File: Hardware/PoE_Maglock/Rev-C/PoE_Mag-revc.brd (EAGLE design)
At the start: 91.8 x 45.4 mm, 82 parts, among them IC2 ATMEGA32U4-MU, J2 1X2-3.5MM, J3 1X2-3.5MM, J4 1X2-3.5MM, J5 1X2-3.5MM, J6 10103594-0001LF, Q1 35A/25V/8.5mΩ, Q3 35A/25V/8.5mΩ, Q5 35A/25V/8.5mΩ, Q6 35A/25V/8.5mΩ, SW1 SPST_TACT-KMR2, T1 DMG3415U, U2 SPX3819-3.3, U3 LMV358IDGKR, U4 W5500, U6 V_REG_317DPACK, X2 J1011FHANRUN, Y4 8MHz

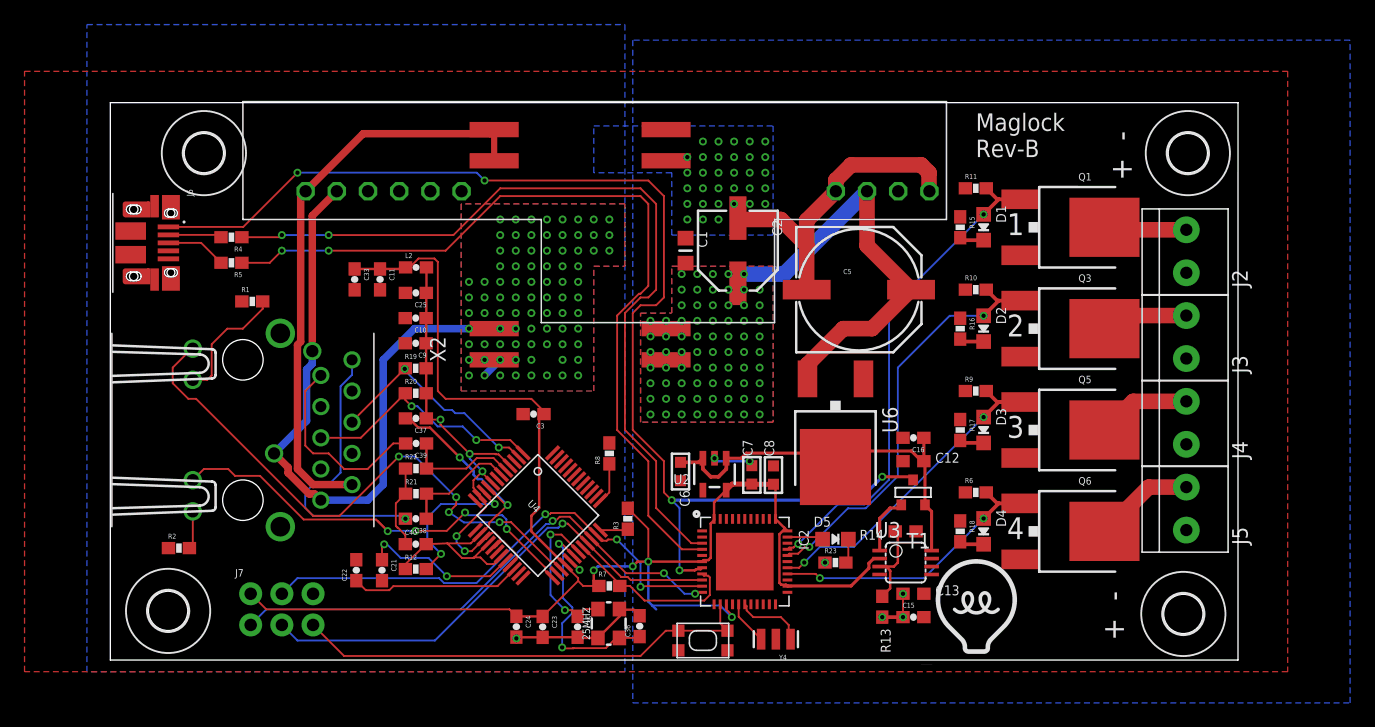
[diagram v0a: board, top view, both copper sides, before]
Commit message: almost done with maglock, adjusted PoE tDocu footprint
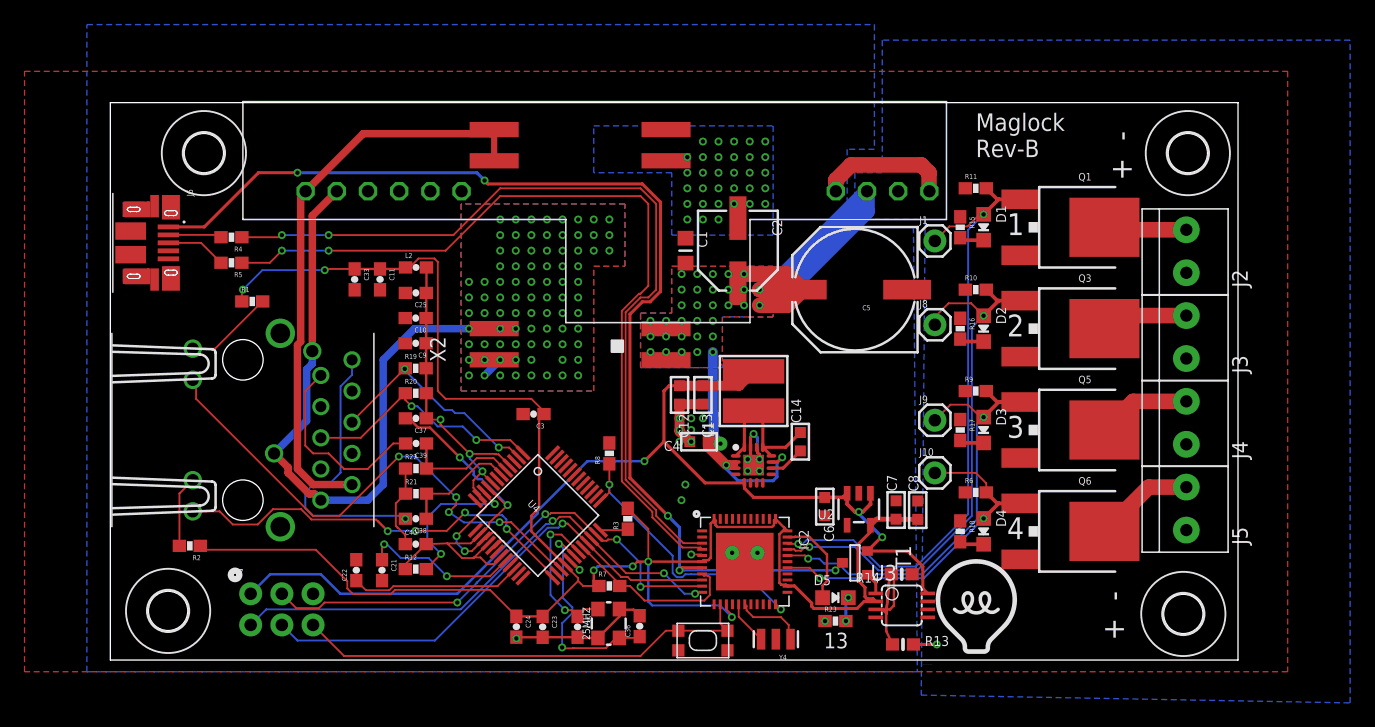
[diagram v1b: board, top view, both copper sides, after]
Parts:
- removed C15, C16: 10uF, SparkFun-Passives:0603-CAP
- removed U6: V_REG_317DPACK, SparkFun-IC-Power:V-REG_DPACK
- added C14: 22nF, microbuilder:0603-MINI
- added C4: 10µF 50V, microbuilder:0603-MINI
- added J1, J10, J8, J9: (no value), SparkFun-Connectors:1X01
- added L1: 4.7uH, microbuilder:INDUCTOR_5X5MM_TDK_VLC5045
- added U$19: BUCK_CONVERTER, Heep:QFN-16
- C12, C13: value 0.1uF -> 22uF 10V; device microbuilder:0603-NO -> microbuilder:0603-MINI
- moved C13 23.6 mm to (48.9, 21.9), turned to 270 degrees
- moved C12 19.8 mm to (47.0, 21.9), turned to 270 degrees
- moved C7 12.1 mm to (64.6, 12.5)
- moved U2 12.1 mm to (61.6, 12.6)
- moved C6 12.1 mm to (58.8, 12.8)
- moved C8 12.1 mm to (66.4, 12.5)
- moved T1 7.44 mm to (61.3, 8.26), turned to 270 degrees
- moved R23 4.76 mm to (59.7, 3.49)
- moved D5 4.76 mm to (59.7, 5.40)
- moved U3 3.51 mm to (65.1, 4.76)
- moved R14 3.51 mm to (65.1, 7.30)
- moved R13 3.51 mm to (65.2, 1.59), turned to 0 degrees
- moved R2 0.91 mm to (7.11, 9.62), turned to 180 degrees
- moved C5 0.32 mm to (61.3, 30.5), turned to 180 degrees
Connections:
- removed net 5: IC2.31
- removed net WIZ_RST_WIZ: R8.1, U4.37
- new net N$14: C14.1, U$19.P10
- new net N$15: C14.2, L1.P$1, U$19.P1, U$19.P12, U$19.P13, U$19.P16
- net +3V3: now also R1.1, R2.1; no longer J7.2
- net +5V: now also C12.1, C13.1, J7.2, L1.P$2, U$19.P5; no longer C12.2, C16.1, U6.4
- net ACTLED: now also X2.12; no longer X2.11
- net EN1: now also IC2.31, J1.1; no longer IC2.30
- net EN2: now also IC2.30, J8.1; no longer IC2.29
- net EN3: now also IC2.29, J9.1; no longer IC2.27
- net EN4: now also IC2.27, J10.1; no longer IC2.26
- net GND: now also C12.2, C4.2, U$19.P14, U$19.P15, U$19.P4, U$19.PAD; no longer C12.1, C15.2, C16.2, R1.1, R2.1, U6.1
- net LNKLED: now also X2.14; no longer X2.13
- net N$3: now also X2.13; no longer X2.14
- net N$4: now also X2.11; no longer X2.12
- net VBAT: now also C4.1, U$19.P11, U$19.P2, U$19.P3; no longer C13.1, C15.1, U6.3
- net WIZ_RST: now also R8.1, U4.37
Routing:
- net +5V: track 33.2 -> 86.4 mm, vias 0 -> 3
- net VBAT: track 38.0 -> 62.7 mm, vias 76 -> 36
- net +3V3: track 130.6 -> 155.1 mm, vias 4 -> 6
- net WIZ_RST: track 0.00 -> 23.5 mm, vias 0 -> 2
- net N$15: track 0.00 -> 12.1 mm
- net EN1: track 40.3 -> 52.3 mm
- net EN2: track 34.1 -> 44.8 mm
- net EN3: track 27.6 -> 37.9 mm
- net GND: track 75.6 -> 67.1 mm, vias 39 -> 54
- net VBUS: track 99.5 -> 91.4 mm
- net CMP: track 7.06 -> 14.2 mm
- net EN4: track 23.0 -> 28.5 mm
- net 13: track 2.93 -> 7.49 mm
- net ACTLED: track 47.0 -> 42.6 mm
- net WIZ_RST_WIZ: track 3.33 -> 0.00 mm
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
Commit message: ready for dylan review
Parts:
- added J11, J12: (no value), SparkFun-Connectors:1X04
- added J13: (no value), SparkFun-Connectors:1X04_NO_SILK
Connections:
- net +3V3: now also J12.1, J12.2, J12.3, J12.4
- net A0: now also J13.4
- net A1: now also J13.3
- net A2: now also J13.2
- net A3: now also J13.1
- net GND: now also J11.1, J11.2, J11.3, J11.4
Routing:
- net A3: track 0.00 -> 20.0 mm, vias 0 -> 1
- net +3V3: track 155.1 -> 173.0 mm
- net A2: track 0.00 -> 15.8 mm, vias 0 -> 1
- net A1: track 0.00 -> 12.4 mm, vias 0 -> 1
- net A0: track 0.00 -> 11.2 mm, vias 0 -> 1
- net GND: vias 54 -> 55
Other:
- board text added: "Maglock Rev-C"
- board text removed: "Maglock Rev-B"
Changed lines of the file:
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@@
 <setting verticaltext="up"/>
 </settings>
-<grid distance="0.15875" unitdist="mm" unit="mm" style="lines" multiple="1" display="no" altdistance="0.15875" altunitdist="mm" altunit="mm"/>
+<grid distance="0.003125" unitdist="mic" unit="mm" style="lines" multiple="1" display="no" altdistance="0.15875" altunitdist="mm" altunit="mm"/>
 <layers>
 <layer number="1" name="Top" color="4" fill="1" visible="yes" active="yes"/>
@@
 <text x="83.82" y="39.37" size="1.778" layer="21" rot="R90">+  -</text>
 <text x="71.12" y="41.275" size="1.4224" layer="21">Maglock
-Rev-B</text>
+Rev-C</text>
 <circle x="10.795" y="7.25" radius="0.25" width="0.7" layer="21"/>
 <text x="58.7375" y="1.27" size="1.27" layer="21" font="fixed" ratio="10" distance="100">13</text>
@@
 <element name="J9" library="SparkFun-Connectors" package="1X01" value="" x="67.78625" y="19.84375"/>
 <element name="J10" library="SparkFun-Connectors" package="1X01" value="" x="67.78625" y="15.5575"/>
+<element name="J11" library="SparkFun-Connectors" package="1X04" value="" x="64.77" y="16.1925" rot="R90">
+<attribute name="PROD_ID" value="CONN-09696" x="64.77" y="16.1925" size="1.778" layer="27" rot="R90" display="off"/>
+</element>
+<element name="J12" library="SparkFun-Connectors" package="1X04" value="" x="59.69" y="16.1925" rot="R90">
+<attribute name="PROD_ID" value="CONN-09696" x="59.69" y="16.1925" size="1.778" layer="27" rot="R90" display="off"/>
+</element>
+<element name="J13" library="SparkFun-Connectors" package="1X04_NO_SILK" value="" x="62.23" y="23.8125" rot="R270">
+<attribute name="PROD_ID" value="CONN-09696" x="62.23" y="23.8125" size="1.778" layer="27" rot="R270" display="off"/>
+</element>
 </elements>
 <signals>
@@
 <via x="47.14875" y="13.335" extent="1-16" drill="0.35"/>
 <via x="47.46625" y="14.605" extent="1-16" drill="0.35"/>
+<contactref element="J11" pad="4"/>
+<contactref element="J11" pad="3"/>
+<contactref element="J11" pad="2"/>
+<contactref element="J11" pad="1"/>
+<via x="56.605040625" y="11.79225625" extent="1-16" drill="0.35"/>
 </signal>
 <signal name="RD-">
@@
 <signal name="A3">
 <contactref element="IC2" pad="39"/>
+<contactref element="J13" pad="1"/>
+<via x="51.634425" y="13.98578125" extent="1-16" drill="0.35"/>
+<wire x1="51.634425" y1="13.98578125" x2="52.21554375" y2="14.5669" width="0.1524" layer="16"/>
+<wire x1="52.21554375" y1="14.5669" x2="54.7573" y2="14.5669" width="0.1524" layer="16"/>
+<wire x1="54.7573" y1="14.5669" x2="56.74471875" y2="16.55431875" width="0.1524" layer="16"/>
+<wire x1="56.74471875" y1="16.55431875" x2="56.74471875" y2="21.530740625" width="0.1524" layer="16"/>
+<wire x1="56.74471875" y1="21.530740625" x2="57.858078125" y2="22.6441" width="0.1524" layer="16"/>
+<wire x1="57.858078125" y1="22.6441" x2="60.17396875" y2="22.6441" width="0.1524" layer="16"/>
+<wire x1="61.34236875" y1="23.8125" x2="62.23" y2="23.8125" width="0.1524" layer="16"/>
+<wire x1="60.17396875" y1="22.6441" x2="61.34236875" y2="23.8125" width="0.1524" layer="16"/>
+<wire x1="52.3065125" y1="11.8075" x2="52.268146875" y2="11.845865625" width="0.1524" layer="1"/>
+<wire x1="52.268146875" y1="11.845865625" x2="52.268146875" y2="12.362459375" width="0.1524" layer="1"/>
+<wire x1="52.268146875" y1="12.362459375" x2="51.634425" y2="12.99618125" width="0.1524" layer="1"/>
+<wire x1="51.634425" y1="12.99618125" x2="51.634425" y2="13.98578125" width="0.1524" layer="1"/>
 </signal>
 <signal name="A2">
 <contactref element="IC2" pad="38"/>
+<contactref element="J13" pad="2"/>
+<via x="52.4965625" y="13.03754375" extent="1-16" drill="0.35"/>
+<wire x1="54.88355625" y1="14.2621" x2="57.541925" y2="16.92046875" width="0.1524" layer="16"/>
+<wire x1="57.541925" y1="16.92046875" x2="57.541925" y2="19.077096875" width="0.1524" layer="16"/>
+<wire x1="57.541925" y1="19.077096875" x2="58.568928125" y2="20.1041" width="0.1524" layer="16"/>
+<wire x1="58.568928125" y1="20.1041" x2="60.17396875" y2="20.1041" width="0.1524" layer="16"/>
+<wire x1="61.34236875" y1="21.2725" x2="62.23" y2="21.2725" width="0.1524" layer="16"/>
+<wire x1="60.17396875" y1="20.1041" x2="61.34236875" y2="21.2725" width="0.1524" layer="16"/>
+<wire x1="52.8065125" y1="11.8075" x2="52.6601125" y2="11.9539" width="0.1524" layer="1"/>
+<wire x1="52.4965625" y1="12.5651125" x2="52.4965625" y2="13.03754375" width="0.1524" layer="1"/>
+<wire x1="52.6601125" y1="11.9539" x2="52.6601125" y2="12.4015625" width="0.1524" layer="1"/>
+<wire x1="52.6601125" y1="12.4015625" x2="52.4965625" y2="12.5651125" width="0.1524" layer="1"/>
+<wire x1="52.4965625" y1="13.03754375" x2="53.72111875" y2="14.2621" width="0.1524" layer="16"/>
+<wire x1="53.72111875" y1="14.2621" x2="54.88355625" y2="14.2621" width="0.1524" layer="16"/>
 </signal>
 <signal name="A1">
 <contactref element="IC2" pad="37"/>
+<contactref element="J13" pad="3"/>
+<via x="53.377059375" y="12.893246875" extent="1-16" drill="0.35"/>
+<wire x1="61.34236875" y1="18.7325" x2="62.23" y2="18.7325" width="0.1524" layer="16"/>
+<wire x1="60.17396875" y1="17.5641" x2="61.34236875" y2="18.7325" width="0.1524" layer="16"/>
+<wire x1="58.6166125" y1="17.5641" x2="60.17396875" y2="17.5641" width="0.1524" layer="16"/>
+<wire x1="55.0098125" y1="13.9573" x2="58.6166125" y2="17.5641" width="0.1524" layer="16"/>
+<wire x1="53.3065125" y1="11.8075" x2="53.3065125" y2="12.835096875" width="0.1524" layer="1"/>
+<wire x1="53.3065125" y1="12.835096875" x2="53.377059375" y2="12.893246875" width="0.1524" layer="1"/>
+<wire x1="53.377059375" y1="12.893246875" x2="54.428715625" y2="13.9573" width="0.1524" layer="16"/>
+<wire x1="54.428715625" y1="13.9573" x2="55.0098125" y2="13.9573" width="0.1524" layer="16"/>
 </signal>
 <signal name="11">
@@
 <wire x1="49.9291125" y1="11.6849" x2="49.8065125" y2="11.8075" width="0.2" layer="1"/>
 <wire x1="54.5360625" y1="11.1551" x2="50.0769625" y2="11.1551" width="0.2" layer="1"/>
+<contactref element="J12" pad="4"/>
+<contactref element="J12" pad="1"/>
+<contactref element="J12" pad="2"/>
+<contactref element="J12" pad="3"/>
+<wire x1="59.69" y1="16.1925" x2="59.69" y2="18.7325" width="0.254" layer="1"/>
+<wire x1="59.69" y1="18.7325" x2="59.69" y2="21.2725" width="0.254" layer="1"/>
+<wire x1="59.69" y1="21.2725" x2="59.69" y2="23.8125" width="0.254" layer="1"/>
+<wire x1="64.40761875" y1="11.772175" x2="63.423871875" y2="12.755921875" width="0.254" layer="1"/>
+<wire x1="64.40761875" y1="11.772175" x2="64.6429375" y2="11.772175" width="0.254" layer="1"/>
+<wire x1="63.423871875" y1="15.662159375" x2="63.4492" y2="15.6874875" width="0.254" layer="1"/>
+<wire x1="63.4492" y1="15.6874875" x2="63.4492" y2="17.00103125" width="0.254" layer="1"/>
+<wire x1="63.4492" y1="17.00103125" x2="63.0061375" y2="17.44409375" width="0.254" layer="1"/>
+<wire x1="63.0061375" y1="17.44409375" x2="60.97840625" y2="17.44409375" width="0.254" layer="1"/>
+<wire x1="60.97840625" y1="17.44409375" x2="59.69" y2="18.7325" width="0.254" layer="1"/>
+<wire x1="63.423871875" y1="12.755921875" x2="63.423871875" y2="15.662159375" width="0.254" layer="1"/>
 </signal>
 <signal name="13">
@@
 <signal name="A0">
 <contactref element="IC2" pad="36"/>
+<contactref element="J13" pad="4"/>
+<via x="55.694796875" y="12.88223125" extent="1-16" drill="0.35"/>
+<wire x1="61.34236875" y1="16.1925" x2="62.23" y2="16.1925" width="0.1524" layer="16"/>
+<wire x1="60.17396875" y1="15.0241" x2="61.34236875" y2="16.1925" width="0.1524" layer="16"/>
+<wire x1="55.694796875" y1="12.88223125" x2="56.861928125" y2="15.0241" width="0.1524" layer="16"/>
+<wire x1="56.861928125" y1="15.0241" x2="60.17396875" y2="15.0241" width="0.1524" layer="16"/>
+<wire x1="53.8065125" y1="11.8075" x2="53.8065125" y2="12.526325" width="0.1524" layer="1"/>
+<wire x1="54.40135625" y1="13.12116875" x2="53.8065125" y2="12.526325" width="0.1524" layer="1"/>
+<wire x1="55.694796875" y1="12.88223125" x2="55.455859375" y2="13.12116875" width="0.1524" layer="1"/>
+<wire x1="55.455859375" y1="13.12116875" x2="54.40135625" y2="13.12116875" width="0.1524" layer="1"/>
 </signal>
 <signal name="3">

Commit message: HEEP-651 updated capacitor voltage ratings to reflect true minimum requirements
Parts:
- C4: value 10µF 50V -> 10µF 25V
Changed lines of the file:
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@@
 </element>
 <element name="U$19" library="Heep" package="QFN-16" value="BUCK_CONVERTER" x="53.0225" y="16.1925"/>
-<element name="C4" library="microbuilder" package="0603-MINI" value="10µF 50V" x="48.5775" y="18.0975" rot="R180"/>
+<element name="C4" library="microbuilder" package="0603-MINI" value="10µF 25V" x="48.5775" y="18.0975" rot="R180"/>
 <element name="C12" library="microbuilder" package="0603-MINI" value="22uF 10V" x="46.99" y="21.9075" rot="R270"/>
 <element name="C13" library="microbuilder" package="0603-MINI" value="22uF 10V" x="48.895" y="21.9075" rot="R270"/>
